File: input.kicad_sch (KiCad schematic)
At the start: 2 parts, among them J1 IEC_60320_C8_Receptacle

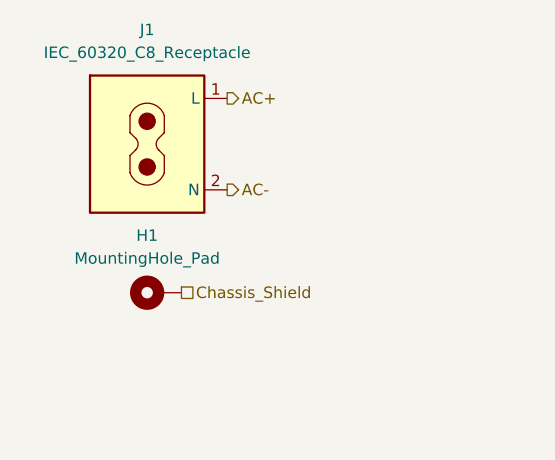
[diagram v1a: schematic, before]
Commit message: updated components
New ganfet selected and further work developing the rp2040 microcontroller circuit
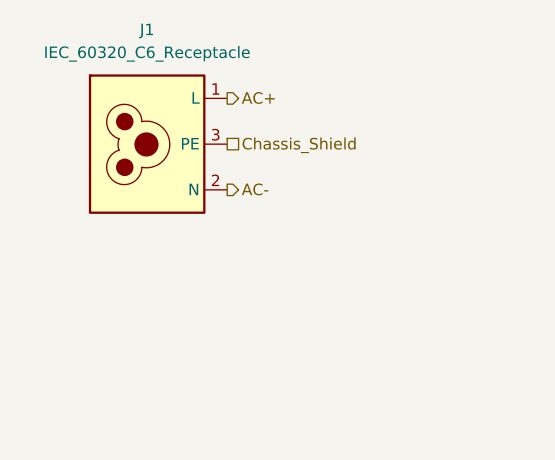
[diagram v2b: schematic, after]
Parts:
- removed H1: MountingHole_Pad, MountingHole:MountingHole_3.2mm_M3_Pad, symbol Mechanical:MountingHole_Pad
- removed J1: IEC_60320_C8_Receptacle, RAPC322X:SWITCHCRAFT_RAPC322X, symbol Connector:IEC_60320_C8_Receptacle
- added J1: IEC_60320_C6_Receptacle, IEC_60320_C6:IEC_60320_C6, symbol Connector:IEC_60320_C6_Receptacle
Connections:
- net AC+: now also J1.1 (L)
- net AC-: now also J1.2 (N)
- net Chassis_Shield: now also J1.3 (PE)
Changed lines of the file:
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@@
 	(hierarchical_label "Chassis_Shield"
 		(shape passive)
-		(at 156.21 92.71 0)
+		(at 161.29 76.2 0)
 		(effects
 			(font
@@
 	)
 	(symbol
-		(lib_id "Connector:IEC_60320_C8_Receptacle")
+		(lib_id "Connector:IEC_60320_C6_Receptacle")
 		(at 152.4 76.2 0)
 		(unit 1)
@@
 			)
 		)
-		(property "Value" "IEC_60320_C8_Receptacle"
+		(property "Value" "IEC_60320_C6_Receptacle"
 			(at 152.4 66.04 0)
 			(effects
@@
 			)
 		)
-		(property "Footprint" "RAPC322X:SWITCHCRAFT_RAPC322X"
+		(property "Footprint" "IEC_60320_C6:IEC_60320_C6"
+			(at 150.5462 76.2376 0)
+			(effects
+				(font
+					(size 1.27 1.27)
+				)
+				(hide yes)
+			)
+		)
+		(property "Datasheet" "~"
+			(at 150.5462 76.2376 0)
+			(effects
+				(font
+					(size 1.27 1.27)
+				)
+				(hide yes)
+			)
+		)
+		(property "Description" "C6 plug, 2,5A max"
 			(at 152.4 76.2 0)
 			(effects
@@
 			)
 		)
-		(property "Datasheet" "~"
-			(at 152.4 76.2 0)
-			(effects
-				(font
-					(size 1.27 1.27)
-				)
-				(hide yes)
-			)
-		)
-		(property "Description" "C8 coupler, 2,5 A max"
-			(at 152.4 76.2 0)
-			(effects
-				(font
-					(size 1.27 1.27)
-				)
-				(hide yes)
-			)
-		)
-		(property "Part Number" ""
-			(at 152.4 76.2 0)
-			(effects
-				(font
-					(size 1.27 1.27)
-				)
-			)
-		)
 		(pin "1"
 		)
 		(pin "2"
+		)
+		(pin "3"
 		)
 		(instances
@@
 					(unit 1)
 				)
-			)
-		)
-	)
-	(symbol
-		(lib_id "Mechanical:MountingHole_Pad")
-		(at 153.67 92.71 90)
-		(unit 1)
-		(exclude_from_sim yes)
-		(in_bom no)
-		(on_board yes)
-		(dnp no)
-		(fields_autoplaced yes)
-		(property "Reference" "H1"
-			(at 152.4 86.36 90)
-			(effects
-				(font
-					(size 1.27 1.27)
-				)
-			)
-		)
-		(property "Value" "MountingHole_Pad"
-			(at 152.4 88.9 90)
-			(effects
-				(font
-					(size 1.27 1.27)
-				)
-			)
-		)
-		(property "Footprint" "MountingHole:MountingHole_3.2mm_M3_Pad"
-			(at 153.67 92.71 0)
-			(effects
-				(font
-					(size 1.27 1.27)
-				)
-				(hide yes)
-			)
-		)
-		(property "Datasheet" "~"
-			(at 153.67 92.71 0)
-			(effects
-				(font
-					(size 1.27 1.27)
-				)
-				(hide yes)
-			)
-		)
-		(property "Description" "Mounting Hole with connection"
-			(at 153.67 92.71 0)
-			(effects
-				(font
-					(size 1.27 1.27)
-				)
-				(hide yes)
-			)
-		)
-		(property "Part Number" ""
-			(at 153.67 92.71 0)
-			(effects
-				(font
-					(size 1.27 1.27)
-				)
-			)
-		)
-		(pin "1"
-		)
-		(instances
-			(project ""
-				(path "/c27c9155-8dca-4b9f-ac37-1fd4cce6afa0/fd71a373-9cb2-456b-bc52-5872eac88a20"
-					(reference "H1")
-					(unit 1)
-				)

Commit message: finished board
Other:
- moved on the sheet: J1
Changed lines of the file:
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@@
 	(title_block
 		(title "Replacable LED COB Lamp")
-		(date "2025-03-24")
+		(date "2025-04-08")
 		(rev "0")
 		(company "WPI ECE2799 D25")
@@
 	(hierarchical_label "AC+"
 		(shape output)
-		(at 161.29 71.12 0)
+		(at 162.56 96.52 0)
 		(fields_autoplaced yes)
 		(effects
@@
 		)
 		(property "Netclass" "HV"
-			(at 161.29 72.39 0)
+			(at 162.56 97.79 0)
 			(effects
 				(font
@@
 	(hierarchical_label "Chassis_Shield"
 		(shape passive)
-		(at 161.29 76.2 0)
+		(at 162.56 101.6 0)
 		(effects
 			(font
@@
 	(hierarchical_label "AC-"
 		(shape output)
-		(at 161.29 81.28 0)
+		(at 162.56 106.68 0)
 		(fields_autoplaced yes)
 		(effects
@@
 		)
 		(property "Netclass" "HV"
-			(at 161.29 82.55 0)
+			(at 162.56 107.95 0)
 			(effects
 				(font
@@
 	(symbol
 		(lib_id "Connector:IEC_60320_C6_Receptacle")
-		(at 152.4 76.2 0)
+		(at 153.67 101.6 0)
 		(unit 1)
 		(exclude_from_sim no)
@@
 		(fields_autoplaced yes)
 		(property "Reference" "J1"
-			(at 152.4 63.5 0)
+			(at 153.67 88.9 0)
 			(effects
 				(font
@@
 		)
 		(property "Value" "IEC_60320_C6_Receptacle"
-			(at 152.4 66.04 0)
+			(at 153.67 91.44 0)
 			(effects
 				(font
@@
 		)
 		(property "Footprint" "IEC_60320_C6:IEC_60320_C6"
-			(at 150.5462 76.2376 0)
+			(at 151.8162 101.6376 0)
 			(effects
 				(font
@@
 		)
 		(property "Datasheet" "~"
-			(at 150.5462 76.2376 0)
+			(at 151.8162 101.6376 0)
 			(effects
 				(font
@@
 		)
 		(property "Description" "C6 plug, 2,5A max"
-			(at 152.4 76.2 0)
+			(at 153.67 101.6 0)
 			(effects
 				(font

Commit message: production design files
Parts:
- J1: Part Number (none) -> 486-4031-ND
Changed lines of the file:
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@@
 			)
 		)
-		(property "Datasheet" "~"
+		(property "Datasheet" "https://www.schurter.com/en/datasheet/typ_2562.pdf"
 			(at 151.8162 101.6376 0)
 			(effects
@@
 			(at 153.67 101.6 0)
 			(effects
+				(font
+					(size 1.27 1.27)
+				)
+				(hide yes)
+			)
+		)
+		(property "Part Number" "486-4031-ND"
+			(at 153.67 101.6 0)
+			(effects

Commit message: board interconnects
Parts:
- added J7, J8: Spade Terminal, 1212:1212, symbol Connector:Conn_01x01_Pin
- added S2: 471001264142, 471001264142:471001264142_0_75-1_25_, symbol 471001264142:471001264142
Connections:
- net AC+: now also J8.1 (Pin_1), S2.2; no longer J1.1 (L)
- new net AC+_in: J1.1 (L), J7.1 (Pin_1), S2.1
